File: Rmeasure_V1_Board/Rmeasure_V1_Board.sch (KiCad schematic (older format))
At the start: 58 parts, among them J1 SWD, J2 USB_B_Micro, J3 CON_CAN, J4 CON_CAN, SW1 RST, SW2 BOOT, U1 STM32F042K6Tx, U2 NCP1117-3.3_SOT223, U3 SN65HVD232, U4 FT230XQ, Y1 8MHz

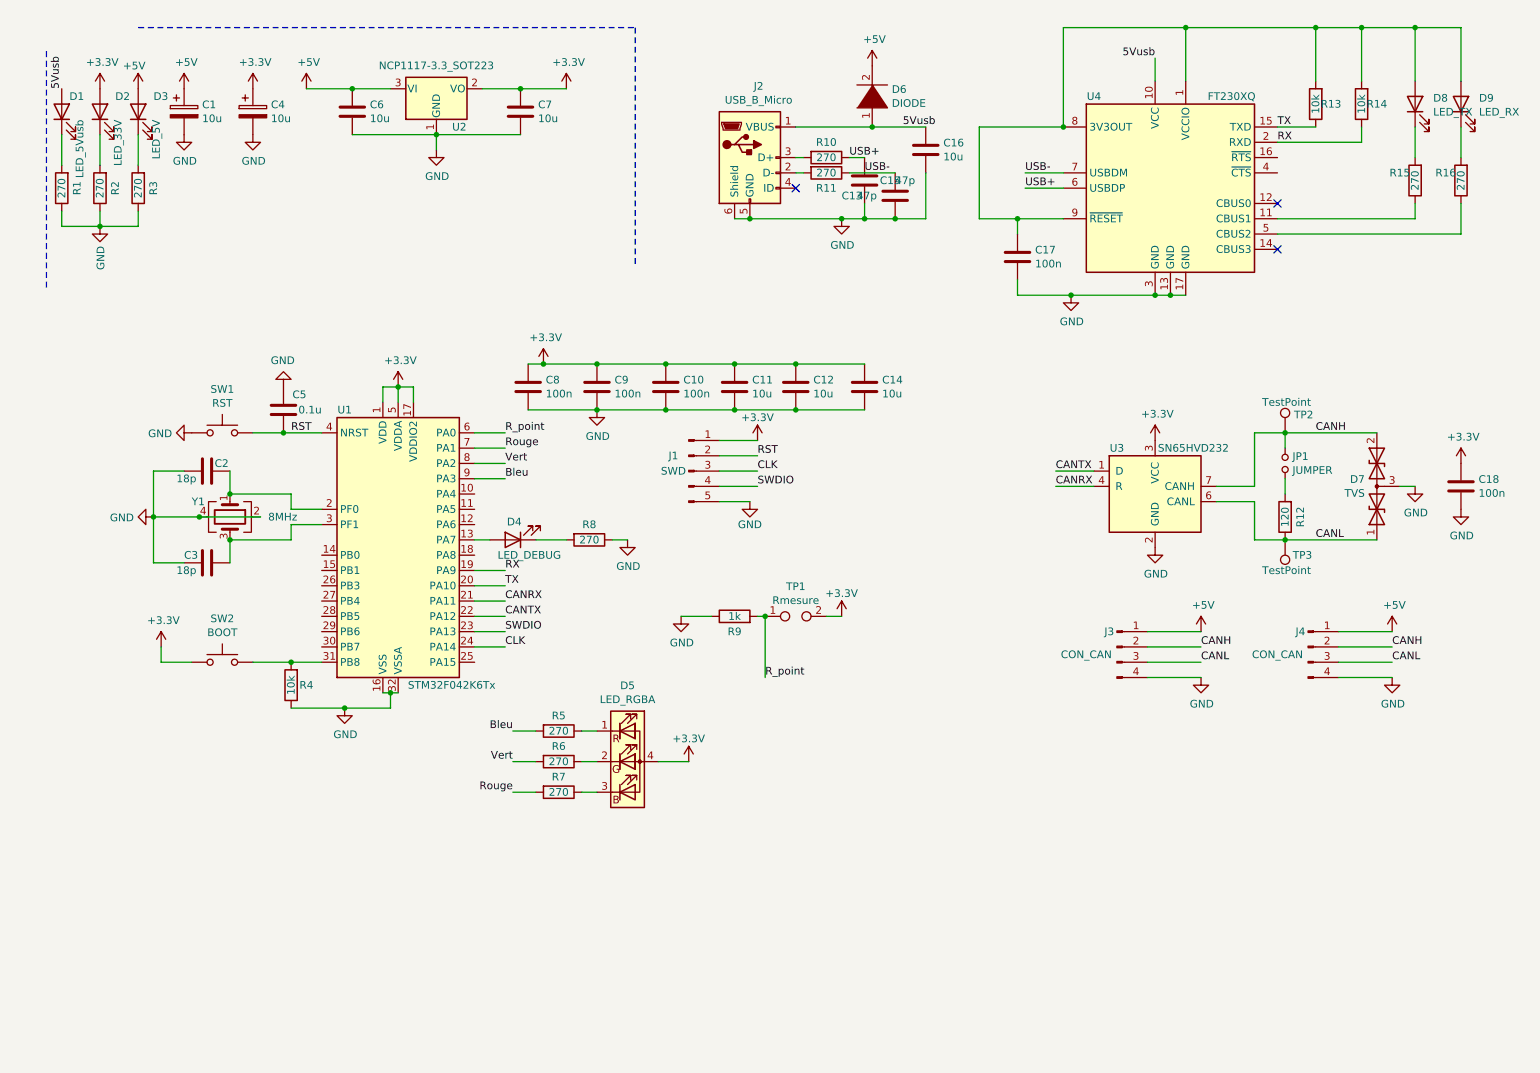
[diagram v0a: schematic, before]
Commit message: Add Rmeasure, Teensy AX12 and main PCB for the CDR2022
-Rmeasure put in production on 13/10
-Add UART to main pcb and rerouting can bus and swap tx/rx pin for the XBEE
-new pcb with teensy 3.2, AX-12 connectivity, UART and CANbus
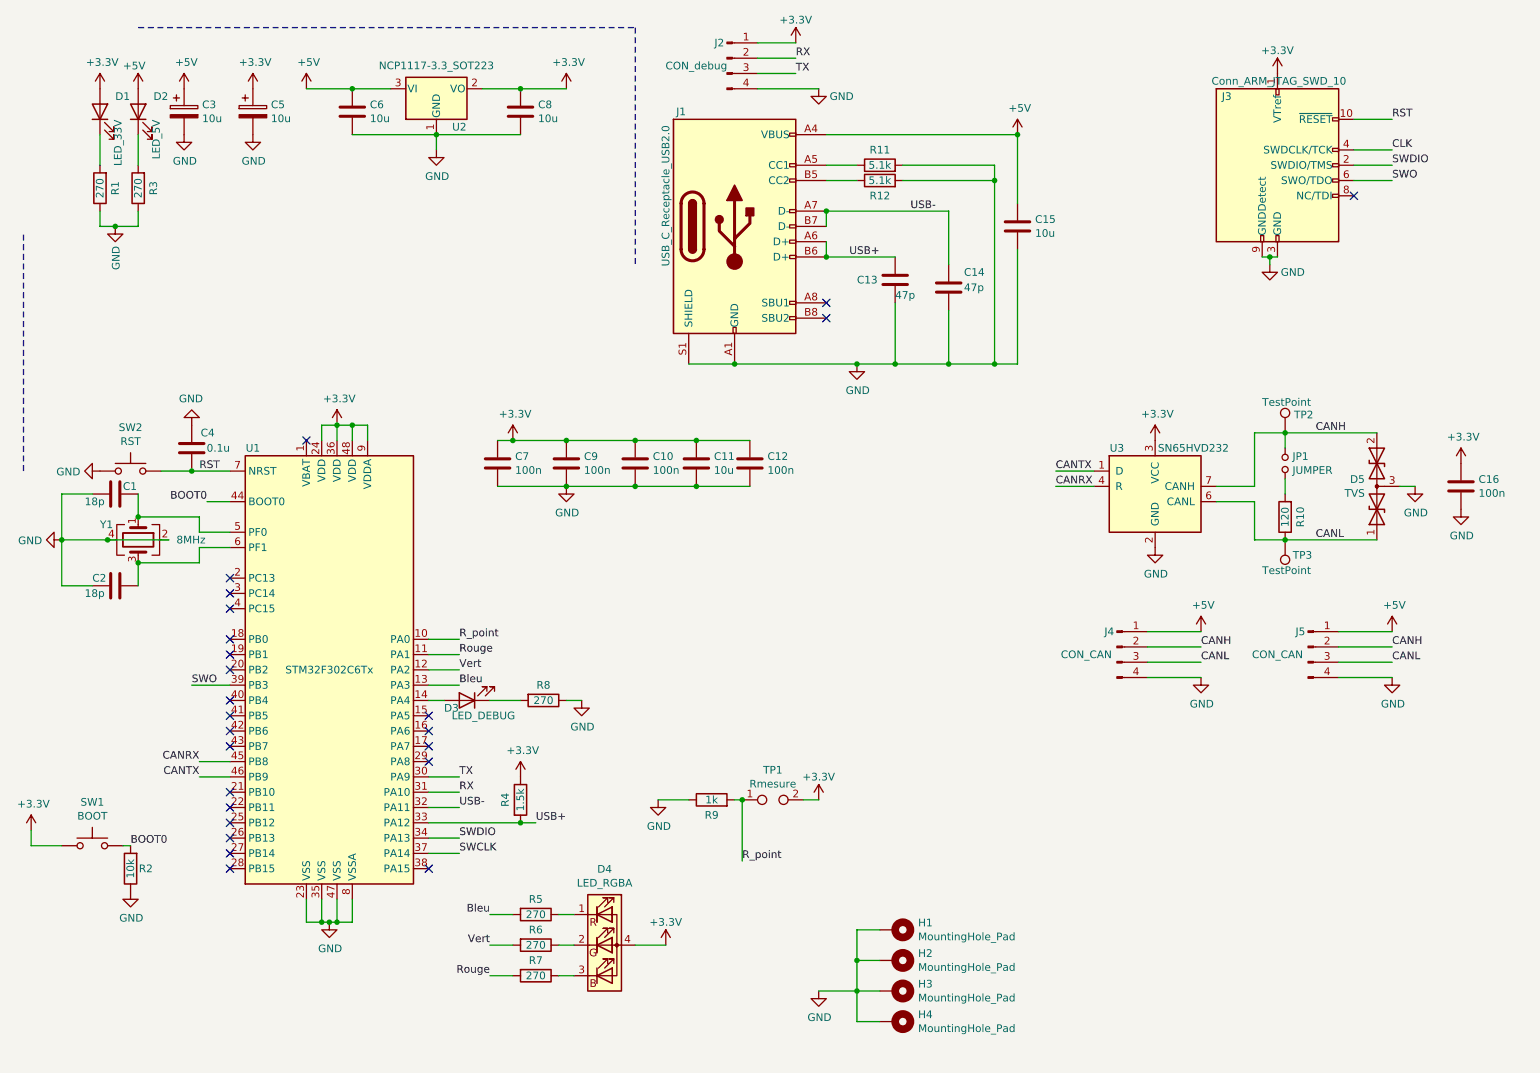
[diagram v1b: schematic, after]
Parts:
- removed C14: 10u, Capacitor_SMD:C_0805_2012Metric, symbol Device:C
- removed C17: 100n, Capacitor_SMD:C_0805_2012Metric, symbol Device:C
- removed D1: LED_5Vusb, LED_SMD:LED_0805_2012Metric, symbol Device:LED
- removed D6: DIODE, Diode_SMD:D_SOD-323_HandSoldering, symbol pspice:DIODE
- removed D8: LED_TX, LED_SMD:LED_0805_2012Metric, symbol Device:LED
- removed D9: LED_RX, LED_SMD:LED_0805_2012Metric, symbol Device:LED
- removed J1: SWD, Connector_PinHeader_2.54mm:PinHeader_1x05_P2.54mm_Vertical, symbol Connector:Conn_01x05_Male
- removed J2: USB_B_Micro, Connector_USB:USB_Micro-B_Wuerth_629105150521, symbol Connector:USB_B_Micro
- removed R1, R10, R15, R16: 270, Resistor_SMD:R_0805_2012Metric, symbol Device:R
- removed R13, R14: 10k, Resistor_SMD:R_0805_2012Metric, symbol Device:R
- removed U1: STM32F042K6Tx, Package_QFP:LQFP-32_7x7mm_P0.8mm, symbol MCU_ST_STM32F0:STM32F042K6Tx
- removed U4: FT230XQ, Package_DFN_QFN:QFN-16-1EP_4x4mm_P0.65mm_EP2.1x2.1mm, symbol Interface_USB:FT230XQ
- added H1, H2, H3, H4: MountingHole_Pad, MountingHole:MountingHole_3.2mm_M3_Pad_Via, symbol Mechanical:MountingHole_Pad
- added J1: USB_C_Receptacle_USB2.0, Connector_USB:USB_C_Receptacle_GCT_USB4085, symbol Connector:USB_C_Receptacle_USB2.0
- added J2: CON_debug, AREA_lib_Connector:Wuerth_2mm_4pin_62000411622, symbol Connector:Conn_01x04_Male
- added J3: Conn_ARM_JTAG_SWD_10, Connector_PinHeader_1.27mm:PinHeader_2x05_P1.27mm_Vertical, symbol Connector:Conn_ARM_JTAG_SWD_10
- added R12: 5.1k, Resistor_SMD:R_0805_2012Metric, symbol Device:R
- added R4: 1.5k, Resistor_SMD:R_0805_2012Metric, symbol Device:R
- added U1: STM32F302C6Tx, Package_QFP:LQFP-48_7x7mm_P0.5mm, symbol MCU_ST_STM32F3:STM32F302C6Tx
- C12: value 10u -> 100n
- D4: renamed from D5; footprint AREA_lib_composant:WL-SFCW_0805 -> LED_SMD:LED_SK6812_EC15_1.5x1.5mm
- R11: value 270 -> 5.1k
- SW1: renamed from SW2; footprint Button_Switch_THT:SW_PUSH_6mm_H5mm -> Button_Switch_SMD:SW_SPST_CK_RS282G05A3
- SW2: renamed from SW1; footprint Button_Switch_THT:SW_PUSH_6mm_H5mm -> Button_Switch_SMD:SW_SPST_CK_RS282G05A3
- TP2, TP3: footprint TestPoint:TestPoint_Plated_Hole_D2.0mm -> TestPoint:TestPoint_Loop_D1.80mm_Drill1.0mm_Beaded
- renumbered C2 to C1, C15 to C14, C16 to C15, C18 to C16, C3 to C2, C1 to C3, C5 to C4, C4 to C5, C8 to C7, C7 to C8, D2 to D1, D3 to D2, D4 to D3, D7 to D5, J3 to J4, J4 to J5, R2 to R1, R12 to R10, R4 to R2
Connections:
- net 5Vusb is gone; now on net +5V: C15.1
- net +3V3: now also J2.1 (Pin_1), J3.1 (VTref), R4.1, U1.24 (VDD), U1.36 (VDD), U1.48 (VDD), U1.9 (VDDA)
- net +5V: now also J1.A4 (VBUS), J1.A9 (VBUS), J1.B4 (VBUS), J1.B9 (VBUS)
- net Bleu: now also U1.13 (PA3)
- net CANRX: now also U1.45 (PB8)
- net CANTX: now also U1.46 (PB9)
- net CLK: now also J3.4 (SWDCLK/TCK)
- net GND: now also R11.2, H1.1, H2.1, H3.1, H4.1, J1.A1 (GND), J1.A12 (GND), J1.B1 (GND), J1.B12 (GND), J1.S1 (SHIELD), J2.4 (Pin_4), J3.3 (GND), J3.5 (GND), J3.9 (GNDDetect), R12.2, U1.23 (VSS), U1.35 (VSS), U1.47 (VSS), U1.8 (VSSA)
- net RST: now also J3.10 (~RESET~), U1.7 (NRST)
- net RX: now also J2.2 (Pin_2), U1.31 (PA10)
- net R_point: now also U1.10 (PA0)
- net Rouge: now also U1.11 (PA1)
- net SWDIO: now also J3.2 (SWDIO/TMS), U1.34 (PA13)
- net TX: now also J2.3 (Pin_3), U1.30 (PA9)
- net USB+: now also J1.A6 (D+), J1.B6 (D+), R4.2, U1.33 (PA12)
- net USB-: now also J1.A7 (D-), J1.B7 (D-), U1.32 (PA11); no longer R11.1
- net Vert: now also U1.12 (PA2)
- net at D3.2 (A): now also U1.14 (PA4)
- net at C1.1, Y1.1: now also U1.5 (PF0)
- net at C2.1, Y1.3: now also U1.6 (PF1)
- net BOOT0: now reaches R2.2, SW1.2
- net BOOT0: now also U1.44 (BOOT0)
- new net: J1.A5 (CC1), R11.1
- new net: J1.B5 (CC2), R12.1
- new net SWCLK: U1.37 (PA14)
- new net SWO: J3.6 (SWO/TDO), U1.39 (PB3)
- no-connect marks 3 -> 25
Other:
- moved on the sheet: C1, C10, C13, C14, C15, C2, C4, C7, C9, D3, D4, R2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

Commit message: ajout v3 carte alim
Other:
- moved on the sheet: D4, H1, H2, H3, H4, R5, R6, R7, R9, TP1
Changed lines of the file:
@@
 L Device:R R9
 U 1 1 617A6532
-P 5000 5750
-F 0 "R9" V 4900 5750 50  0000 C CNN
-F 1 "1k" V 5000 5750 50  0000 C CNN
-F 2 "Resistor_SMD:R_0805_2012Metric" V 4930 5750 50  0001 C CNN
-F 3 "~" H 5000 5750 50  0001 C CNN
-	1    5000 5750
+P 5500 5150
+F 0 "R9" V 5400 5150 50  0000 C CNN
+F 1 "1k" V 5500 5150 50  0000 C CNN
+F 2 "Resistor_SMD:R_0805_2012Metric" V 5430 5150 50  0001 C CNN
+F 3 "~" H 5500 5150 50  0001 C CNN
+	1    5500 5150
 	0    -1   -1   0
 $EndComp
@@
 L power:+3.3V #PWR027
 U 1 1 617A8FD6
-P 5700 5750
-F 0 "#PWR027" H 5700 5600 50  0001 C CNN
-F 1 "+3.3V" H 5700 5900 50  0000 C CNN
-F 2 "" H 5700 5750 50  0001 C CNN
-F 3 "" H 5700 5750 50  0001 C CNN
-	1    5700 5750
-	1    0    0    -1
-$EndComp
-Wire Wire Line
-	4650 5750 4850 5750
+P 6200 5150
+F 0 "#PWR027" H 6200 5000 50  0001 C CNN
+F 1 "+3.3V" H 6200 5300 50  0000 C CNN
+F 2 "" H 6200 5150 50  0001 C CNN
+F 3 "" H 6200 5150 50  0001 C CNN
+	1    6200 5150
+	1    0    0    -1
+$EndComp
+Wire Wire Line
+	5150 5150 5350 5150
 Wire Wire Line
 	3600 3700 4050 3700
 Wire Wire Line
-	5150 5750 5200 5750
+	5650 5150 5700 5150
 $Comp
 L Connector:TestPoint_2Pole TP1
 U 1 1 617B76A0
-P 5400 5750
-F 0 "TP1" H 5400 5945 50  0000 C CNN
-F 1 "Rmesure" H 5400 5854 50  0000 C CNN
-F 2 "TestPoint:TestPoint_Pad_4.0x4.0mm" H 5400 5750 50  0001 C CNN
-F 3 "~" H 5400 5750 50  0001 C CNN
-	1    5400 5750
-	1    0    0    -1
-$EndComp
-Wire Wire Line
-	5600 5750 5700 5750
+P 5900 5150
+F 0 "TP1" H 5900 5345 50  0000 C CNN
+F 1 "Rmesure" H 5900 5254 50  0000 C CNN
+F 2 "TestPoint:TestPoint_Pad_4.0x4.0mm" H 5900 5150 50  0001 C CNN
+F 3 "~" H 5900 5150 50  0001 C CNN
+	1    5900 5150
+	1    0    0    -1
+$EndComp
+Wire Wire Line
+	6100 5150 6200 5150
 $Comp
 L power:GND #PWR022
 U 1 1 617C164E
-P 4650 5750
-F 0 "#PWR022" H 4650 5500 50  0001 C CNN
-F 1 "GND" H 4655 5577 50  0000 C CNN
-F 2 "" H 4650 5750 50  0001 C CNN
-F 3 "" H 4650 5750 50  0001 C CNN
-	1    4650 5750
-	1    0    0    -1
-$EndComp
-Wire Wire Line
-	5200 5750 5200 6150
-Connection ~ 5200 5750
-Text Label 5200 6150 0    50   ~ 0
+P 5150 5150
+F 0 "#PWR022" H 5150 4900 50  0001 C CNN
+F 1 "GND" H 5155 4977 50  0000 C CNN
+F 2 "" H 5150 5150 50  0001 C CNN
+F 3 "" H 5150 5150 50  0001 C CNN
+	1    5150 5150
+	1    0    0    -1
+$EndComp
+Wire Wire Line
+	5700 5150 5700 5550
+Connection ~ 5700 5150
+Text Label 5700 5550 0    50   ~ 0
 R_point
 Wire Wire Line
@@
 L Device:R R5
 U 1 1 617EC642
-P 3850 6500
-F 0 "R5" V 3750 6500 50  0000 C CNN
-F 1 "270" V 3850 6500 50  0000 C CNN
-F 2 "Resistor_SMD:R_0805_2012Metric" V 3780 6500 50  0001 C CNN
-F 3 "~" H 3850 6500 50  0001 C CNN
-	1    3850 6500
+P 3750 6950
+F 0 "R5" V 3650 6950 50  0000 C CNN
+F 1 "270" V 3750 6950 50  0000 C CNN
+F 2 "Resistor_SMD:R_0805_2012Metric" V 3680 6950 50  0001 C CNN
+F 3 "~" H 3750 6950 50  0001 C CNN
+	1    3750 6950
 	0    1    1    0
 $EndComp
@@
 L Device:R R6
 U 1 1 617ED869
-P 3850 6700
-F 0 "R6" V 3750 6700 50  0000 C CNN
-F 1 "270" V 3850 6700 50  0000 C CNN
-F 2 "Resistor_SMD:R_0805_2012Metric" V 3780 6700 50  0001 C CNN
-F 3 "~" H 3850 6700 50  0001 C CNN
-	1    3850 6700
+P 3750 7150
+F 0 "R6" V 3650 7150 50  0000 C CNN
+F 1 "270" V 3750 7150 50  0000 C CNN
+F 2 "Resistor_SMD:R_0805_2012Metric" V 3680 7150 50  0001 C CNN
+F 3 "~" H 3750 7150 50  0001 C CNN
+	1    3750 7150
 	0    1    1    0
 $EndComp
@@
 L Device:R R7
 U 1 1 617EDE60
-P 3850 6900
-F 0 "R7" V 3750 6900 50  0000 C CNN
-F 1 "270" V 3850 6900 50  0000 C CNN
-F 2 "Resistor_SMD:R_0805_2012Metric" V 3780 6900 50  0001 C CNN
-F 3 "~" H 3850 6900 50  0001 C CNN
-	1    3850 6900
-	0    1    1    0
-$EndComp
-Wire Wire Line
-	4000 6500 4100 6500
-Wire Wire Line
-	4000 6700 4100 6700
-Wire Wire Line
-	4000 6900 4100 6900
-Wire Wire Line
-	3550 6500 3700 6500
-Wire Wire Line
-	3700 6700 3550 6700
-Wire Wire Line
-	3700 6900 3550 6900
-Text Label 3550 6900 2    50   ~ 0
+P 3750 7350
+F 0 "R7" V 3650 7350 50  0000 C CNN
+F 1 "270" V 3750 7350 50  0000 C CNN
+F 2 "Resistor_SMD:R_0805_2012Metric" V 3680 7350 50  0001 C CNN
+F 3 "~" H 3750 7350 50  0001 C CNN
+	1    3750 7350
+	0    1    1    0
+$EndComp
+Wire Wire Line
+	3900 6950 4000 6950
+Wire Wire Line
+	3900 7150 4000 7150
+Wire Wire Line
+	3900 7350 4000 7350
+Wire Wire Line
+	3450 6950 3600 6950
+Wire Wire Line
+	3600 7150 3450 7150
+Wire Wire Line
+	3600 7350 3450 7350
+Text Label 3450 7350 2    50   ~ 0
 Rouge
-Text Label 3550 6700 2    50   ~ 0
+Text Label 3450 7150 2    50   ~ 0
 Vert
-Text Label 3550 6500 2    50   ~ 0
+Text Label 3450 6950 2    50   ~ 0
 Bleu
 Wire Wire Line
-	4500 6700 4700 6700
+	4400 7150 4600 7150
 $Comp
 L Device:LED_RGBA D4
 U 1 1 61698EB2
-P 4300 6700
-F 0 "D4" H 4300 7197 50  0000 C CNN
-F 1 "LED_RGBA" H 4300 7106 50  0000 C CNN
-F 2 "LED_SMD:LED_SK6812_EC15_1.5x1.5mm" H 4300 6650 50  0001 C CNN
-F 3 "~" H 4300 6650 50  0001 C CNN
-	1    4300 6700
+P 4200 7150
+F 0 "D4" H 4200 7647 50  0000 C CNN
+F 1 "LED_RGBA" H 4200 7556 50  0000 C CNN
+F 2 "LED_SMD:LED_SK6812_EC15_1.5x1.5mm" H 4200 7100 50  0001 C CNN
+F 3 "~" H 4200 7100 50  0001 C CNN
+	1    4200 7150
 	1    0    0    -1
 $EndComp
@@
 L power:+3.3V #PWR023
 U 1 1 61699C32
-P 4700 6700
-F 0 "#PWR023" H 4700 6550 50  0001 C CNN
-F 1 "+3.3V" H 4700 6850 50  0000 C CNN
-F 2 "" H 4700 6700 50  0001 C CNN
-F 3 "" H 4700 6700 50  0001 C CNN
-	1    4700 6700
+P 4600 7150
+F 0 "#PWR023" H 4600 7000 50  0001 C CNN
+F 1 "+3.3V" H 4600 7300 50  0000 C CNN
+F 2 "" H 4600 7150 50  0001 C CNN
+F 3 "" H 4600 7150 50  0001 C CNN
+	1    4600 7150
 	1    0    0    -1
 $EndComp
@@
 L Mechanical:MountingHole_Pad H1
 U 1 1 616ACCC9
-P 6200 6600
-F 0 "H1" V 6154 6750 50  0000 L CNN
-F 1 "MountingHole_Pad" V 6245 6750 50  0000 L CNN
-F 2 "MountingHole:MountingHole_3.2mm_M3_Pad_Via" H 6200 6600 50  0001 C CNN
-F 3 "~" H 6200 6600 50  0001 C CNN
-	1    6200 6600
+P 6100 6600
+F 0 "H1" V 6054 6750 50  0000 L CNN
+F 1 "MountingHole_Pad" V 6145 6750 50  0000 L CNN
+F 2 "MountingHole:MountingHole_3.2mm_M3_Pad_Via" H 6100 6600 50  0001 C CNN
+F 3 "~" H 6100 6600 50  0001 C CNN
+	1    6100 6600
 	0    1    1    0
 $EndComp
@@
 L Mechanical:MountingHole_Pad H2
 U 1 1 616ADA50
-P 6200 6800
-F 0 "H2" V 6154 6950 50  0000 L CNN
-F 1 "MountingHole_Pad" V 6245 6950 50  0000 L CNN
-F 2 "MountingHole:MountingHole_3.2mm_M3_Pad_Via" H 6200 6800 50  0001 C CNN
-F 3 "~" H 6200 6800 50  0001 C CNN
-	1    6200 6800
+P 6100 6800
+F 0 "H2" V 6054 6950 50  0000 L CNN
+F 1 "MountingHole_Pad" V 6145 6950 50  0000 L CNN
+F 2 "MountingHole:MountingHole_3.2mm_M3_Pad_Via" H 6100 6800 50  0001 C CNN
+F 3 "~" H 6100 6800 50  0001 C CNN
+	1    6100 6800
 	0    1    1    0
 $EndComp
@@
 L Mechanical:MountingHole_Pad H3
 U 1 1 616ADFFD
-P 6200 7000
-F 0 "H3" V 6154 7150 50  0000 L CNN
-F 1 "MountingHole_Pad" V 6245 7150 50  0000 L CNN
-F 2 "MountingHole:MountingHole_3.2mm_M3_Pad_Via" H 6200 7000 50  0001 C CNN
-F 3 "~" H 6200 7000 50  0001 C CNN
-	1    6200 7000
+P 6100 7000
+F 0 "H3" V 6054 7150 50  0000 L CNN
+F 1 "MountingHole_Pad" V 6145 7150 50  0000 L CNN
+F 2 "MountingHole:MountingHole_3.2mm_M3_Pad_Via" H 6100 7000 50  0001 C CNN
+F 3 "~" H 6100 7000 50  0001 C CNN
+	1    6100 7000
 	0    1    1    0
 $EndComp
@@
 L Mechanical:MountingHole_Pad H4
 U 1 1 616AE5C5
-P 6200 7200
-F 0 "H4" V 6154 7350 50  0000 L CNN
-F 1 "MountingHole_Pad" V 6245 7350 50  0000 L CNN
-F 2 "MountingHole:MountingHole_3.2mm_M3_Pad_Via" H 6200 7200 50  0001 C CNN
-F 3 "~" H 6200 7200 50  0001 C CNN
-	1    6200 7200
+P 6100 7200
+F 0 "H4" V 6054 7350 50  0000 L CNN
+F 1 "MountingHole_Pad" V 6145 7350 50  0000 L CNN
+F 2 "MountingHole:MountingHole_3.2mm_M3_Pad_Via" H 6100 7200 50  0001 C CNN
+F 3 "~" H 6100 7200 50  0001 C CNN
+	1    6100 7200
 	0    1    1    0
 $EndComp
@@
 L power:GND #PWR040
 U 1 1 616AEB46
-P 5700 7000
-F 0 "#PWR040" H 5700 6750 50  0001 C CNN
-F 1 "GND" H 5705 6827 50  0000 C CNN
-F 2 "" H 5700 7000 50  0001 C CNN
-F 3 "" H 5700 7000 50  0001 C CNN
-	1    5700 7000
-	1    0    0    -1
-$EndComp
-Wire Wire Line
-	6100 6600 5950 6600
-Wire Wire Line
-	5950 6600 5950 6800
-Wire Wire Line
-	5950 7200 6100 7200
-Wire Wire Line
-	6100 7000 5950 7000
-Connection ~ 5950 7000
-Wire Wire Line
-	5950 7000 5950 7200
-Wire Wire Line
-	6100 6800 5950 6800
-Connection ~ 5950 6800
-Wire Wire Line
-	5950 6800 5950 7000
-Wire Wire Line
-	5950 7000 5700 7000
+P 5600 7000
+F 0 "#PWR040" H 5600 6750 50  0001 C CNN
+F 1 "GND" H 5605 6827 50  0000 C CNN
+F 2 "" H 5600 7000 50  0001 C CNN
+F 3 "" H 5600 7000 50  0001 C CNN
+	1    5600 7000
+	1    0    0    -1
+$EndComp
+Wire Wire Line
+	6000 6600 5850 6600
+Wire Wire Line
+	5850 6600 5850 6800
+Wire Wire Line
+	5850 7200 6000 7200
+Wire Wire Line
+	6000 7000 5850 7000
+Connection ~ 5850 7000
+Wire Wire Line
+	5850 7000 5850 7200
+Wire Wire Line
+	6000 6800 5850 6800
+Connection ~ 5850 6800
+Wire Wire Line
+	5850 6800 5850 7000
+Wire Wire Line
+	5850 7000 5600 7000
 $Comp
 L Connector:USB_C_Receptacle_USB2.0 J1
